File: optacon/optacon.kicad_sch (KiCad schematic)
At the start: 17 parts, among them J1 Conn_01x12, J2 Conn_01x40_Socket

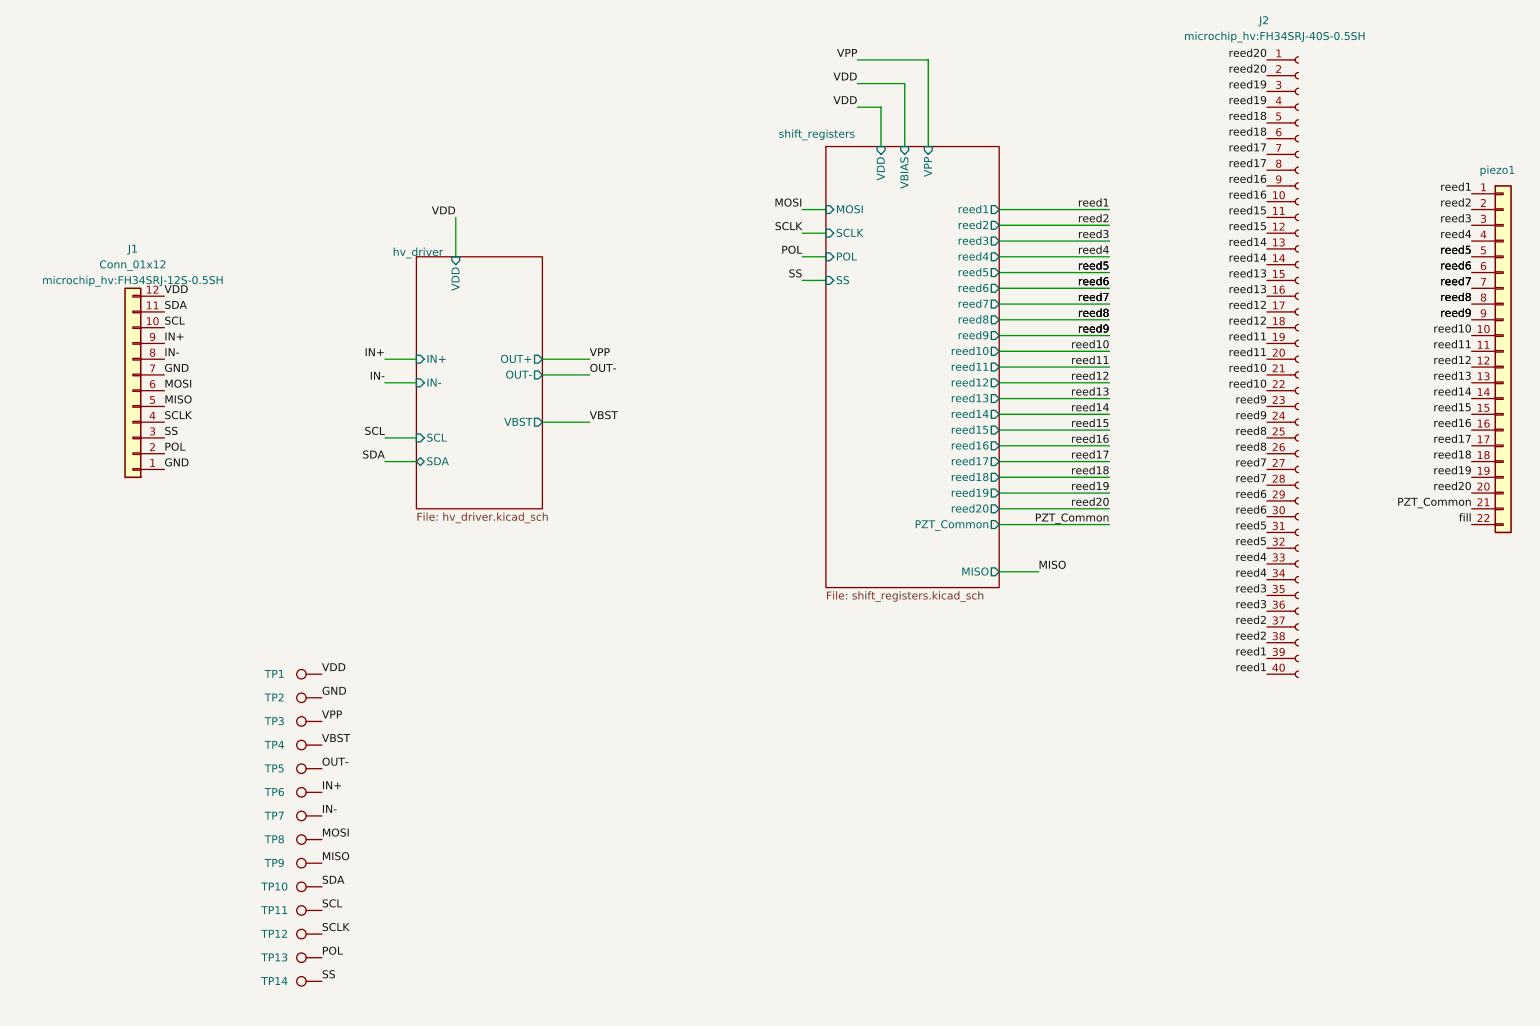
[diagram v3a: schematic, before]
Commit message: separate VIN and VDD
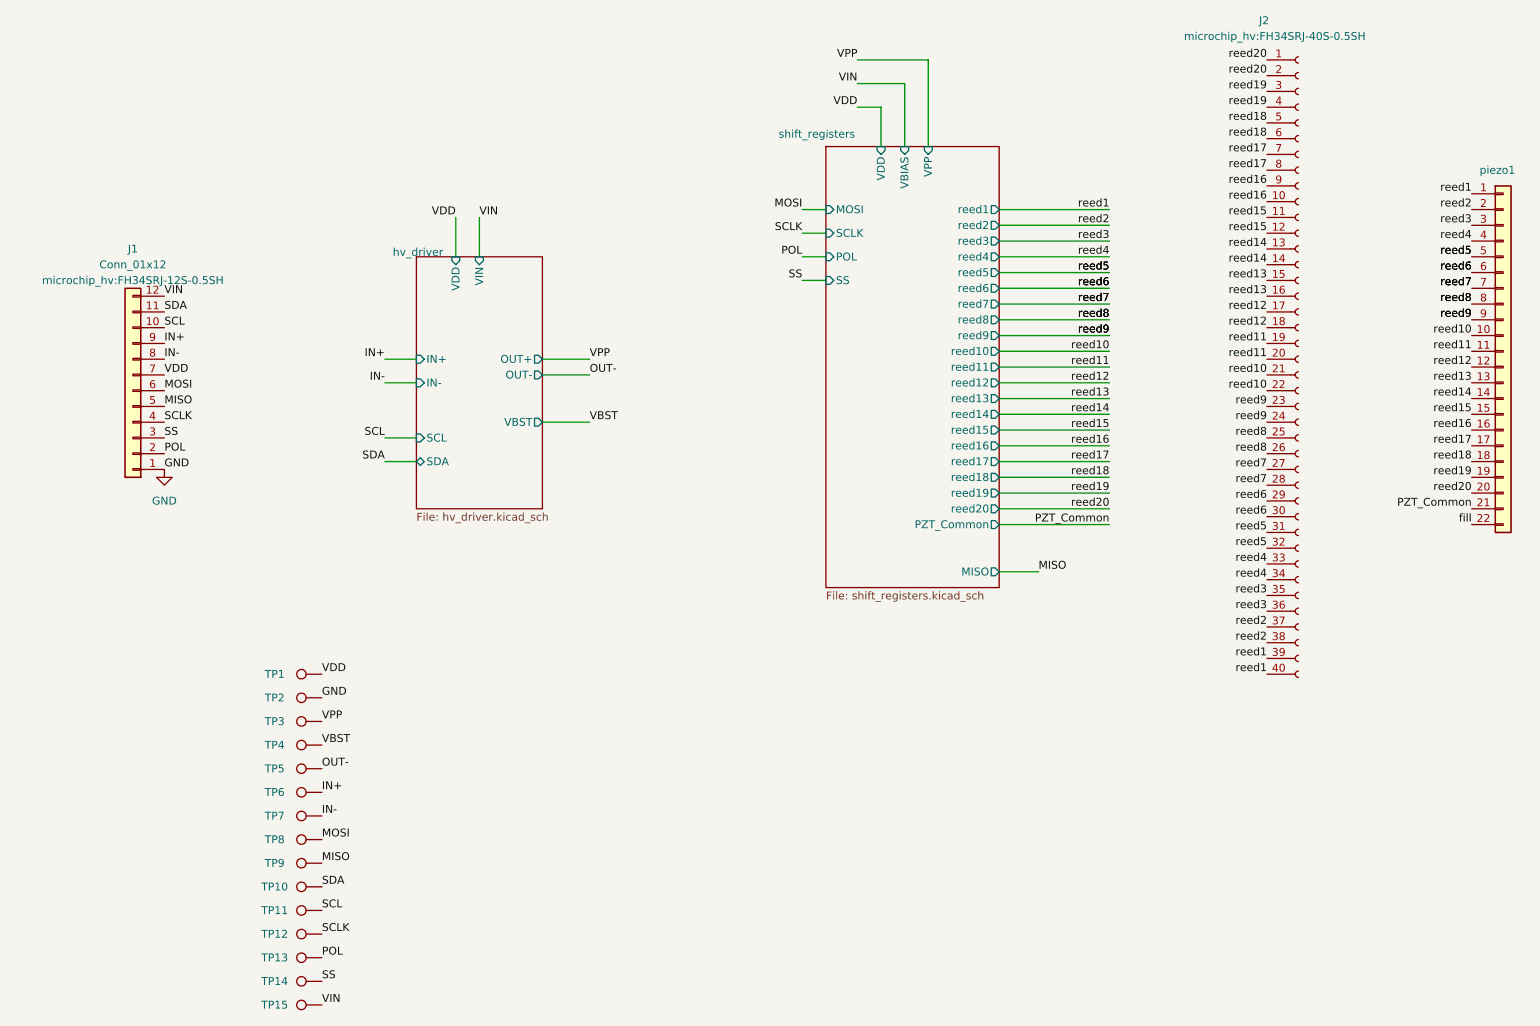
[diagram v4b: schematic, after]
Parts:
- added TP15: VDD, TestPoint:TestPoint_THTPad_D1.0mm_Drill0.5mm, symbol Connector:TestPoint
- TP1: value TestPoint -> VDD
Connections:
- net GND: no longer J1.7 (Pin_7)
- net VDD: now also J1.7 (Pin_7); no longer J1.12 (Pin_12)
- new net VIN: J1.12 (Pin_12), TP15.1
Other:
- sheet hv_driver ports: added VIN; removed none
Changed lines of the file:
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@@
+    (stroke (width 0) (type default))
+  )
+  (wire (pts (xy 114.3 63.5) (xy 114.3 69.85))
+    (stroke (width 0) (type default))
+  )
+  (wire (pts (xy 198.12 102.87) (xy 215.9 102.87))
+    (stroke (width 0) (type default))
+  )
+  (wire (pts (xy 175.26 38.1) (xy 186.69 38.1))
+    (stroke (width 0) (type default))
+  )
+  (wire (pts (xy 198.12 110.49) (xy 215.9 110.49))
+    (stroke (width 0) (type default))
+  )
+  (wire (pts (xy 198.12 62.23) (xy 215.9 62.23))
+    (stroke (width 0) (type default))
+  )
+  (wire (pts (xy 198.12 100.33) (xy 215.9 100.33))
     (stroke (width 0) (type default))
   )
@@
     (stroke (width 0) (type default))
   )
-  (wire (pts (xy 198.12 102.87) (xy 215.9 102.87))
-    (stroke (width 0) (type default))
-  )
-  (wire (pts (xy 175.26 38.1) (xy 186.69 38.1))
-    (stroke (width 0) (type default))
-  )
-  (wire (pts (xy 198.12 110.49) (xy 215.9 110.49))
-    (stroke (width 0) (type default))
-  )
-  (wire (pts (xy 198.12 62.23) (xy 215.9 62.23))
-    (stroke (width 0) (type default))
-  )
-  (wire (pts (xy 198.12 100.33) (xy 215.9 100.33))
-    (stroke (width 0) (type default))
-  )
   (wire (pts (xy 124.46 96.52) (xy 132.08 96.52))
     (stroke (width 0) (type default))
@@
     (effects (font (size 1.27 1.27)) (justify right bottom))
   )
-  (label "GND" (at 63.5 88.9 0) (fields_autoplaced)
+  (label "VDD" (at 63.5 88.9 0) (fields_autoplaced)
     (effects (font (size 1.27 1.27)) (justify left bottom))
   )
@@
     (effects (font (size 1.27 1.27)) (justify right bottom))
   )
+  (label "VIN" (at 88.9 190.5 0) (fields_autoplaced)
+    (effects (font (size 1.27 1.27)) (justify left bottom))
+  )
   (label "reed12" (at 274.32 87.63 180) (fields_autoplaced)
     (effects (font (size 1.27 1.27)) (justify right bottom))
@@
     (effects (font (size 1.27 1.27)) (justify right bottom))
   )
-  (label "VDD" (at 175.26 41.91 180) (fields_autoplaced)
+  (label "VIN" (at 175.26 41.91 180) (fields_autoplaced)
     (effects (font (size 1.27 1.27)) (justify right bottom))
   )
@@
     (effects (font (size 1.27 1.27)) (justify left bottom))
   )
-  (label "VDD" (at 63.5 76.2 0) (fields_autoplaced)
+  (label "VIN" (at 63.5 76.2 0) (fields_autoplaced)
     (effects (font (size 1.27 1.27)) (justify left bottom))
   )
@@
     (effects (font (size 1.27 1.27)) (justify right bottom))
   )
+  (label "VIN" (at 114.3 63.5 0) (fields_autoplaced)
+    (effects (font (size 1.27 1.27)) (justify left bottom))
+  )
+  (label "reed12" (at 215.9 90.17 180) (fields_autoplaced)
+    (effects (font (size 1.27 1.27)) (justify right bottom))
+  )
+  (label "reed8" (at 241.3 99.06 180) (fields_autoplaced)
+    (effects (font (size 1.27 1.27)) (justify right bottom))
+  )
+  (label "reed20" (at 215.9 110.49 180) (fields_autoplaced)
+    (effects (font (size 1.27 1.27)) (justify right bottom))
+  )
+  (label "reed1" (at 241.3 137.16 180) (fields_autoplaced)
+    (effects (font (size 1.27 1.27)) (justify right bottom))
+  )
+  (label "reed17" (at 274.32 100.33 180) (fields_autoplaced)
+    (effects (font (size 1.27 1.27)) (justify right bottom))
+  )
+  (label "SDA" (at 88.9 171.45 0) (fields_autoplaced)
+    (effects (font (size 1.27 1.27)) (justify left bottom))
+  )
+  (label "reed6" (at 241.3 111.76 180) (fields_autoplaced)
+    (effects (font (size 1.27 1.27)) (justify right bottom))
+  )
+  (label "reed18" (at 241.3 48.26 180) (fields_autoplaced)
+    (effects (font (size 1.27 1.27)) (justify right bottom))
+  )
+  (label "MISO" (at 204.47 120.65 0) (fields_autoplaced)
+    (effects (font (size 1.27 1.27)) (justify left bottom))
+  )
+  (label "VDD" (at 88.9 137.16 0) (fields_autoplaced)
+    (effects (font (size 1.27 1.27)) (justify left bottom))
+  )
+  (label "PZT_Common" (at 274.32 110.49 180) (fields_autoplaced)
+    (effects (font (size 1.27 1.27)) (justify right bottom))
+  )
+  (label "fill" (at 274.32 113.03 180) (fields_autoplaced)
+    (effects (font (size 1.27 1.27)) (justify right bottom))
+  )
   (label "VDD" (at 110.49 63.5 180) (fields_autoplaced)
-    (effects (font (size 1.27 1.27)) (justify right bottom))
-  )
-  (label "reed12" (at 215.9 90.17 180) (fields_autoplaced)
-    (effects (font (size 1.27 1.27)) (justify right bottom))
-  )
-  (label "reed8" (at 241.3 99.06 180) (fields_autoplaced)
-    (effects (font (size 1.27 1.27)) (justify right bottom))
-  )
-  (label "reed20" (at 215.9 110.49 180) (fields_autoplaced)
-    (effects (font (size 1.27 1.27)) (justify right bottom))
-  )
-  (label "reed1" (at 241.3 137.16 180) (fields_autoplaced)
-    (effects (font (size 1.27 1.27)) (justify right bottom))
-  )
-  (label "reed17" (at 274.32 100.33 180) (fields_autoplaced)
-    (effects (font (size 1.27 1.27)) (justify right bottom))
-  )
-  (label "SDA" (at 88.9 171.45 0) (fields_autoplaced)
-    (effects (font (size 1.27 1.27)) (justify left bottom))
-  )
-  (label "reed6" (at 241.3 111.76 180) (fields_autoplaced)
-    (effects (font (size 1.27 1.27)) (justify right bottom))
-  )
-  (label "reed18" (at 241.3 48.26 180) (fields_autoplaced)
-    (effects (font (size 1.27 1.27)) (justify right bottom))
-  )
-  (label "MISO" (at 204.47 120.65 0) (fields_autoplaced)
-    (effects (font (size 1.27 1.27)) (justify left bottom))
-  )
-  (label "VDD" (at 88.9 137.16 0) (fields_autoplaced)
-    (effects (font (size 1.27 1.27)) (justify left bottom))
-  )
-  (label "PZT_Common" (at 274.32 110.49 180) (fields_autoplaced)
-    (effects (font (size 1.27 1.27)) (justify right bottom))
-  )
-  (label "fill" (at 274.32 113.03 180) (fields_autoplaced)
     (effects (font (size 1.27 1.27)) (justify right bottom))
   )
@@
     )
   )
-  (symbol (lib_id "Connector:TestPoint") (at 88.9 137.16 90) (unit 1)
+  (symbol (lib_name "TestPoint_1") (lib_id "Connector:TestPoint") (at 88.9 190.5 90) (unit 1)
+    (in_bom yes) (on_board yes) (dnp no)
+    (property "Reference" "TP15" (at 81.28 190.5 90)
+      (effects (font (size 1.27 1.27)))
+    )
+    (property "Value" "VDD" (at 95.25 190.5 90)
+      (effects (font (size 1.27 1.27)) hide)
+    )
+    (property "Footprint" "TestPoint:TestPoint_THTPad_D1.0mm_Drill0.5mm" (at 88.9 185.42 0)
+      (effects (font (size 1.27 1.27)) hide)
+    )
+    (property "Datasheet" "~" (at 88.9 185.42 0)
+      (effects (font (size 1.27 1.27)) hide)
+    )
+    (pin "1")
+    (instances
+      (project "optacon"
+        (path "/e63e39d7-6ac0-4ffd-8aa3-1841a4541b55"
+          (reference "TP15") (unit 1)
+        )
+      )
+    )
+  )
+  (symbol (lib_name "TestPoint_1") (lib_id "Connector:TestPoint") (at 88.9 137.16 90) (unit 1)
     (in_bom yes) (on_board yes) (dnp no)
     (property "Reference" "TP1" (at 81.28 137.16 90)
       (effects (font (size 1.27 1.27)))
     )
-    (property "Value" "TestPoint" (at 95.25 137.16 90)
+    (property "Value" "VDD" (at 95.25 137.16 90)
       (effects (font (size 1.27 1.27)) hide)
     )
@@
         (path "/e63e39d7-6ac0-4ffd-8aa3-1841a4541b55"
           (reference "TP7") (unit 1)
+        )
+      )
+    )
+  )
+  (symbol (lib_id "power:GND") (at 63.5 104.14 0) (unit 1)
+    (in_bom yes) (on_board yes) (dnp no) (fields_autoplaced)
+    (property "Reference" "#PWR04" (at 63.5 110.49 0)
+      (effects (font (size 1.27 1.27)) hide)
+    )
+    (property "Value" "GND" (at 63.5 109.22 0)
+      (effects (font (size 1.27 1.27)))
+    )
+    (property "Footprint" "" (at 63.5 104.14 0)
+      (effects (font (size 1.27 1.27)) hide)
+    )
+    (property "Datasheet" "" (at 63.5 104.14 0)
+      (effects (font (size 1.27 1.27)) hide)
+    )
+    (pin "1")
+    (instances
+      (project "optacon"
+        (path "/e63e39d7-6ac0-4ffd-8aa3-1841a4541b55"
+          (reference "#PWR04") (unit 1)
         )
       )
@@
       (effects (font (size 1.27 1.27)) (justify right))
     )
+    (pin "VIN" input (at 114.3 69.85 90)
+      (effects (font (size 1.27 1.27)) (justify right))
+    )
